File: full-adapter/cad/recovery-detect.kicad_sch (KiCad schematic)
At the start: 6 parts, among them U9 TXU0202DCUR

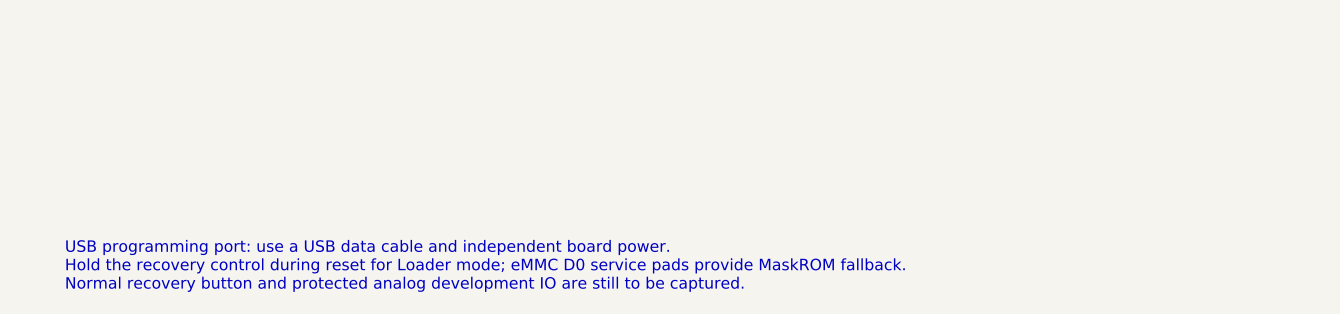
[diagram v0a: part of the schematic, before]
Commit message: Add hardware recovery reset and PMIC power buttons
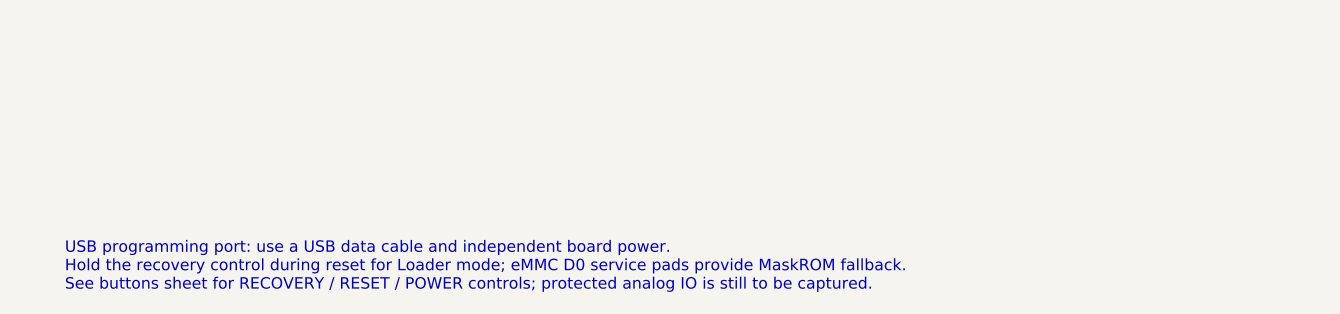
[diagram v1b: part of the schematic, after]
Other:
- note added: "USB programming port: use a USB data cable and independent board power. Hold the recovery control during reset for Loader mode; eMMC D0 service pads provide MaskROM fallback. See buttons sheet for RECOVERY / RESET / POWER controls; protected analog IO is still to be captured."
- note removed: "USB programming port: use a USB data cable and independent board power. Hold the recovery control during reset for Loader mode; eMMC D0 service pads provide MaskROM fallback. Normal recovery button and protected analog development IO are still to be captured."
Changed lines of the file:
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@@
 (pin "1")(instances (project "full-adapter" (path "/fda20879-fa66-56c0-be14-de2506349b46/cc20ce09-055c-5a82-8732-0c9cd00b9c29" (reference "#PWRrecoverydetect010") (unit 1)))))
 (text "No host power is tied to a processor rail. A1 and OE follow connector VBUS.\nB1Y reports VBUS through a divider to the dedicated detector; B2 is tied LOW.\nEither translator supply absent disables its outputs. R635 defines the detector LOW.\n\nQUALIFICATION OPEN: dedicated VBUSDET leakage/LOW threshold, rail tolerance,\npartial-supply behavior, reset timing and USB BootROM operation.\nCalculated HIGH is 2.711–3.198V only under research/recovery-qualification.json assumptions.\nThis circuit is not release-qualified; resolve these bounds before manufacture." (at 17.78 157.48 0) (effects (font (size 1.27 1.27)) (justify left top)))
-(text "USB programming port: use a USB data cable and independent board power.\nHold the recovery control during reset for Loader mode; eMMC D0 service pads provide MaskROM fallback.\nNormal recovery button and protected analog development IO are still to be captured." (at 15.24 233.68 0) (effects (font (size 1.27 1.27)) (justify left top)))
+(text "USB programming port: use a USB data cable and independent board power.\nHold the recovery control during reset for Loader mode; eMMC D0 service pads provide MaskROM fallback.\nSee buttons sheet for RECOVERY / RESET / POWER controls; protected analog IO is still to be captured." (at 15.24 233.68 0) (effects (font (size 1.27 1.27)) (justify left top)))
 )
